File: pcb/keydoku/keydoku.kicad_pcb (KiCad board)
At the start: 2 copper layers, 111 x 99.9 mm, 17 parts

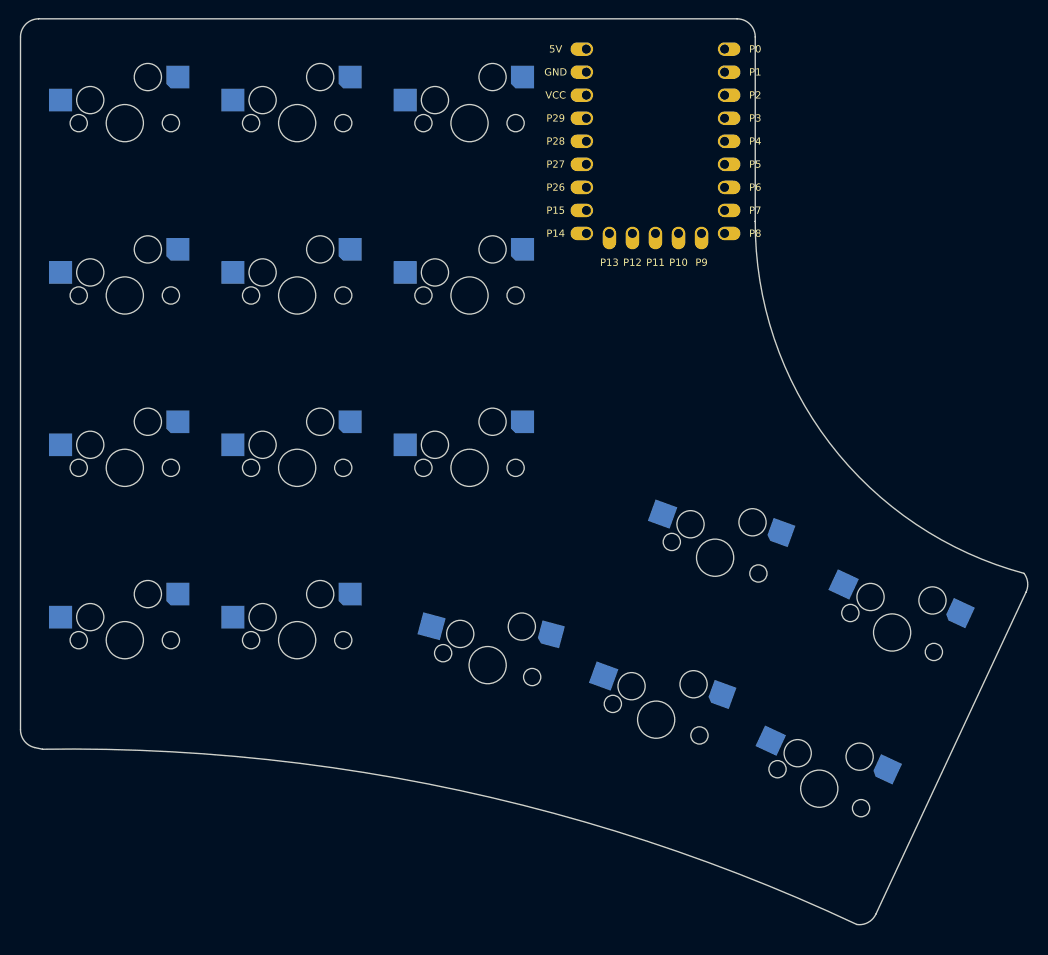
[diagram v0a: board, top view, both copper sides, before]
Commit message: Adding per key LEDs
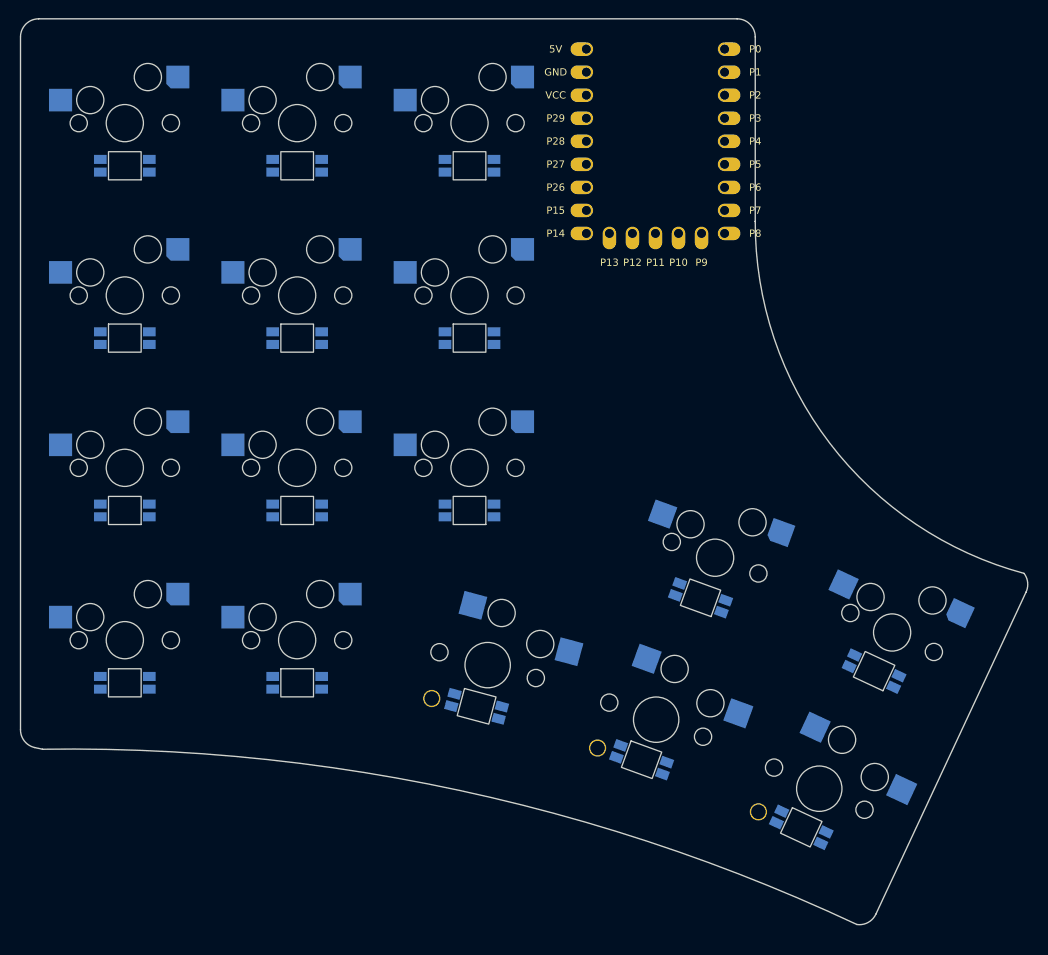
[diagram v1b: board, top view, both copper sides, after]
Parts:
- added LED1: , ceoloide:led_SK6812mini-e (per-keysingle-side), B.Cu at (100.0, 135.7)
- added LED10: , ceoloide:led_SK6812mini-e (per-keysingle-side), B.Cu at (100.0, 116.7)
- added LED11: , ceoloide:led_SK6812mini-e (per-keysingle-side), B.Cu at (119.0, 154.7)
- added LED12: , ceoloide:led_SK6812mini-e (per-keysingle-side), B.Cu at (119.0, 116.7)
- added LED13: , ceoloide:led_SK6812mini-e (per-keysingle-side), B.Cu at (138.0, 116.7)
- added LED14: , ceoloide:led_SK6812mini-e (per-keysingle-side), B.Cu at (138.8, 157.3)
- added LED15: , ceoloide:led_SK6812mini-e (per-keysingle-side), B.Cu at (157.0, 163.2)
- added LED16: , ceoloide:led_SK6812mini-e (per-keysingle-side), B.Cu at (174.6, 170.6)
- added LED2: , ceoloide:led_SK6812mini-e (per-keysingle-side), B.Cu at (100.0, 97.7)
- added LED3: , ceoloide:led_SK6812mini-e (per-keysingle-side), B.Cu at (119.0, 135.7)
- added LED4: , ceoloide:led_SK6812mini-e (per-keysingle-side), B.Cu at (119.0, 97.7)
- added LED5: , ceoloide:led_SK6812mini-e (per-keysingle-side), B.Cu at (138.0, 135.7)
- added LED6: , ceoloide:led_SK6812mini-e (per-keysingle-side), B.Cu at (138.0, 97.7)
- added LED7: , ceoloide:led_SK6812mini-e (per-keysingle-side), B.Cu at (163.5, 145.3)
- added LED8: , ceoloide:led_SK6812mini-e (per-keysingle-side), B.Cu at (182.6, 153.4)
- added LED9: , ceoloide:led_SK6812mini-e (per-keysingle-side), B.Cu at (100.0, 154.7)
- S14, S15, S16: footprint ceoloide:switch_mx -> ceoloide:switch_choc_v1_v2
- moved S12 27.7 mm to (165.1, 140.9), turned to -20 degrees
- moved S14 27.7 mm to (140.0, 152.8), turned to -15 degrees
- moved S13 27.7 mm to (184.6, 149.2), turned to -25 degrees
- moved S15 19.5 mm to (158.6, 158.8), turned to -20 degrees
- moved S16 19.0 mm to (176.6, 166.4)
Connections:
- MCU1 pad 20: P29 -> LED_1
- S1 pad 1: (no net) -> GND
- S1 pad 2: GND -> (no net)
- S10 pad 1: (no net) -> GND
- S10 pad 2: GND -> (no net)
- S11 pad 1: (no net) -> GND
- S11 pad 2: GND -> P2
- S12 pad 1: (no net) -> GND
- S12 pad 2: GND -> (no net)
- S13 pad 1: (no net) -> GND
- S13 pad 2: GND -> (no net)
- S14 pad 1: (no net) -> GND
- S14 pad 2: GND -> (no net)
- S15 pad 1: (no net) -> GND
- S15 pad 2: GND -> (no net)
- S16 pad 1: (no net) -> GND
- S16 pad 2: GND -> (no net)
- S2 pad 1: (no net) -> GND
- S2 pad 2: GND -> (no net)
- S3 pad 1: (no net) -> GND
- S3 pad 2: GND -> (no net)
- S4 pad 1: (no net) -> GND
- S4 pad 2: GND -> (no net)
- S5 pad 1: (no net) -> GND
- S5 pad 2: GND -> (no net)
- S6 pad 1: (no net) -> GND
- S6 pad 2: GND -> (no net)
- S7 pad 1: (no net) -> GND
- S7 pad 2: GND -> (no net)
- S8 pad 1: (no net) -> GND
- S8 pad 2: GND -> (no net)
- S9 pad 1: (no net) -> GND
- S9 pad 2: GND -> (no net)

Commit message: Adding key nets and mounting holes
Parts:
- added H1: , ceoloide:mounting_hole_plated, F.Cu at (100.0, 102.5)
- added H2: , ceoloide:mounting_hole_plated, F.Cu at (138.0, 102.5)
- added H3: , ceoloide:mounting_hole_plated, F.Cu at (100.0, 140.5)
- added H4: , ceoloide:mounting_hole_plated, F.Cu at (171.4, 153.4)
- moved LED14 4.70 mm to (140.0, 152.8)
- moved LED10 4.70 mm to (100.0, 112.0)
- moved LED12 4.70 mm to (119.0, 112.0)
- moved LED13 4.70 mm to (138.0, 112.0)
- moved LED11 4.70 mm to (119.0, 150.0)
- moved LED9 4.70 mm to (100.0, 150.0)
- moved LED15 4.70 mm to (158.6, 158.8)
- moved LED16 4.70 mm to (176.6, 166.4)
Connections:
- S1 pad 2: (no net) -> P9
- S10 pad 2: (no net) -> P13
- S11 pad 2: P2 -> P26
- S12 pad 2: (no net) -> P6
- S13 pad 2: (no net) -> P7
- S14 pad 2: (no net) -> P3
- S15 pad 2: (no net) -> P4
- S16 pad 2: (no net) -> P5
- S2 pad 2: (no net) -> P12
- S3 pad 2: (no net) -> P15
- S4 pad 2: (no net) -> P28
- S5 pad 2: (no net) -> P8
- S6 pad 2: (no net) -> P11
- S7 pad 2: (no net) -> P14
- S8 pad 2: (no net) -> P27
- S9 pad 2: (no net) -> P10
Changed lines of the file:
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@@
 			(chamfer_ratio 0.2)
 			(chamfer bottom_left)
-      (net 0 ""))
+      (net 13 "P9"))
 		(fp_poly
 			(pts
@@
 			(chamfer_ratio 0.2)
 			(chamfer bottom_left)
-      (net 0 ""))
+      (net 16 "P12"))
 		(fp_poly
 			(pts
@@
 			(chamfer_ratio 0.2)
 			(chamfer bottom_left)
-      (net 0 ""))
+      (net 19 "P15"))
 		(fp_poly
 			(pts
@@
 			(chamfer_ratio 0.2)
 			(chamfer bottom_left)
-      (net 0 ""))
+      (net 22 "P28"))
 		(fp_poly
 			(pts
@@
 			(chamfer_ratio 0.2)
 			(chamfer bottom_left)
-      (net 0 ""))
+      (net 12 "P8"))
 		(fp_poly
 			(pts
@@
 			(chamfer_ratio 0.2)
 			(chamfer bottom_left)
-      (net 0 ""))
+      (net 15 "P11"))
 		(fp_poly
 			(pts
@@
 			(chamfer_ratio 0.2)
 			(chamfer bottom_left)
-      (net 0 ""))
+      (net 18 "P14"))
 		(fp_poly
 			(pts
@@
 			(chamfer_ratio 0.2)
 			(chamfer bottom_left)
-      (net 0 ""))
+      (net 21 "P27"))
 		(fp_poly
 			(pts
@@
 			(chamfer_ratio 0.2)
 			(chamfer bottom_left)
-      (net 0 ""))
+      (net 14 "P10"))
 		(fp_poly
 			(pts
@@
 			(chamfer_ratio 0.2)
 			(chamfer bottom_left)
-      (net 0 ""))
+      (net 17 "P13"))
 		(fp_poly
 			(pts
@@
 			(chamfer_ratio 0.2)
 			(chamfer bottom_left)
-      (net 6 "P2"))
+      (net 20 "P26"))
 		(fp_poly
 			(pts
@@
 			(chamfer_ratio 0.2)
 			(chamfer bottom_left)
-      (net 0 ""))
+      (net 10 "P6"))
 		(fp_poly
 			(pts
@@
 			(chamfer_ratio 0.2)
 			(chamfer bottom_left)
-      (net 0 ""))
+      (net 11 "P7"))
 		(fp_poly
 			(pts
@@
     (fp_arc (start 0.8 -3.7) (mid 1.956518 -3.312082) (end 2.5 -2.22) (layer "B.SilkS") (stroke (width 0.15) (type solid)))
     (pad "1" smd rect (at -3.275 -5.95 -15) (size 2.6 2.6) (layers "B.Cu" "B.Paste" "B.Mask") (net 1 "GND"))
-    (pad "2" smd rect (at 8.275 -3.75 -15) (size 2.6 2.6) (layers "B.Cu" "B.Paste" "B.Mask") (net 0 ""))
+    (pad "2" smd rect (at 8.275 -3.75 -15) (size 2.6 2.6) (layers "B.Cu" "B.Paste" "B.Mask") (net 7 "P3"))
     (pad "" np_thru_hole circle (at 5 -3.75 180) (size 3 3) (drill 3) (layers "*.Cu" "*.Mask"))
   )
@@
     (fp_arc (start 0.8 -3.7) (mid 1.956518 -3.312082) (end 2.5 -2.22) (layer "B.SilkS") (stroke (width 0.15) (type solid)))
     (pad "1" smd rect (at -3.275 -5.95 -20) (size 2.6 2.6) (layers "B.Cu" "B.Paste" "B.Mask") (net 1 "GND"))
-    (pad "2" smd rect (at 8.275 -3.75 -20) (size 2.6 2.6) (layers "B.Cu" "B.Paste" "B.Mask") (net 0 ""))
+    (pad "2" smd rect (at 8.275 -3.75 -20) (size 2.6 2.6) (layers "B.Cu" "B.Paste" "B.Mask") (net 8 "P4"))
     (pad "" np_thru_hole circle (at 5 -3.75 175) (size 3 3) (drill 3) (layers "*.Cu" "*.Mask"))
   )
@@
     (fp_arc (start 0.8 -3.7) (mid 1.956518 -3.312082) (end 2.5 -2.22) (layer "B.SilkS") (stroke (width 0.15) (type solid)))
     (pad "1" smd rect (at -3.275 -5.95 -25) (size 2.6 2.6) (layers "B.Cu" "B.Paste" "B.Mask") (net 1 "GND"))
-    (pad "2" smd rect (at 8.275 -3.75 -25) (size 2.6 2.6) (layers "B.Cu" "B.Paste" "B.Mask") (net 0 ""))
+    (pad "2" smd rect (at 8.275 -3.75 -25) (size 2.6 2.6) (layers "B.Cu" "B.Paste" "B.Mask") (net 9 "P5"))
     (pad "" np_thru_hole circle (at 5 -3.75 170) (size 3 3) (drill 3) (layers "*.Cu" "*.Mask"))
   )
@@
   (footprint "ceoloide:led_SK6812mini-e (per-keysingle-side)"
     (layer "B.Cu")
-    (at 100 154.7 0)
+    (at 100 150 0)
     (property "Reference" "LED9"
       (at -4.75 0 90)
@@
   (footprint "ceoloide:led_SK6812mini-e (per-keysingle-side)"
     (layer "B.Cu")
-    (at 100 116.7 0)
+    (at 100 112 0)
     (property "Reference" "LED10"
       (at -4.75 0 90)
@@
   (footprint "ceoloide:led_SK6812mini-e (per-keysingle-side)"
     (layer "B.Cu")
-    (at 119 154.7 0)
+    (at 119 150 0)
     (property "Reference" "LED11"
       (at -4.75 0 90)
@@
   (footprint "ceoloide:led_SK6812mini-e (per-keysingle-side)"
     (layer "B.Cu")
-    (at 119 116.7 0)
+    (at 119 112 0)
     (property "Reference" "LED12"
       (at -4.75 0 90)
@@
   (footprint "ceoloide:led_SK6812mini-e (per-keysingle-side)"
     (layer "B.Cu")
-    (at 138 116.7 0)
+    (at 138 112 0)
     (property "Reference" "LED13"
       (at -4.75 0 90)
@@
   (footprint "ceoloide:led_SK6812mini-e (per-keysingle-side)"
     (layer "B.Cu")
-    (at 138.7835505 157.2898514 -15)
+    (at 140 152.75 -15)
     (property "Reference" "LED14"
       (at -4.75 0 75)
@@
   (footprint "ceoloide:led_SK6812mini-e (per-keysingle-side)"
     (layer "B.Cu")
-    (at 156.96923990000002 163.1794525 -20)
+    (at 158.5767346 158.7628972 -20)
     (property "Reference" "LED15"
       (at -4.75 0 70)
@@
   (footprint "ceoloide:led_SK6812mini-e (per-keysingle-side)"
     (layer "B.Cu")
-    (at 174.57241470000002 170.6316292 -25)
+    (at 176.55872050000002 166.3719826 -25)
     (property "Reference" "LED16"
       (at -4.75 0 65)
@@
     (fp_rect (start -1.8 -1.55) (end 1.8 1.55) (layer "Edge.Cuts") (stroke (width 0.12) (type solid)) (fill none))
   )
+  (footprint "ceoloide:mounting_hole_plated"
+    (layer "F.Cu")
+    (at 100 102.5 0)
+    (property "Reference" "H1"
+      (at 0 3 0)
+      (layer "F.SilkS")
+      hide
+      (effects (font (size 1 1) (thickness 0.15)))
+    )
+    (pad "" thru_hole circle (at 0 0 0) (size 3.8000000000000003 3.8000000000000003) (drill 2.2) (layers "*.Cu" "*.Mask"))
+    (fp_circle (center 0 0) (end -2.1500000000000004 0) (layer "F.CrtYd") (stroke (width 0.05) (type solid)) (fill none))
+    (fp_circle (center 0 0) (end -2.1500000000000004 0) (layer "B.CrtYd") (stroke (width 0.05) (type solid)) (fill none))
+  )
+  (footprint "ceoloide:mounting_hole_plated"
+    (layer "F.Cu")
+    (at 138 102.5 0)
+    (property "Reference" "H2"
+      (at 0 3 0)
+      (layer "F.SilkS")
+      hide
+      (effects (font (size 1 1) (thickness 0.15)))
+    )
+    (pad "" thru_hole circle (at 0 0 0) (size 3.8000000000000003 3.8000000000000003) (drill 2.2) (layers "*.Cu" "*.Mask"))
+    (fp_circle (center 0 0) (end -2.1500000000000004 0) (layer "F.CrtYd") (stroke (width 0.05) (type solid)) (fill none))
+    (fp_circle (center 0 0) (end -2.1500000000000004 0) (layer "B.CrtYd") (stroke (width 0.05) (type solid)) (fill none))
+  )
+  (footprint "ceoloide:mounting_hole_plated"
+    (layer "F.Cu")
+    (at 100 140.5 0)
+    (property "Reference" "H3"
+      (at 0 3 0)
+      (layer "F.SilkS")
+      hide
+      (effects (font (size 1 1) (thickness 0.15)))
+    )
+    (pad "" thru_hole circle (at 0 0 0) (size 3.8000000000000003 3.8000000000000003) (drill 2.2) (layers "*.Cu" "*.Mask"))
+    (fp_circle (center 0 0) (end -2.1500000000000004 0) (layer "F.CrtYd") (stroke (width 0.05) (type solid)) (fill none))
+    (fp_circle (center 0 0) (end -2.1500000000000004 0) (layer "B.CrtYd") (stroke (width 0.05) (type solid)) (fill none))
+  )
+  (footprint "ceoloide:mounting_hole_plated"
+    (layer "F.Cu")
+    (at 171.44 153.42000000000002 0)
+    (property "Reference" "H4"
+      (at 0 3 0)
+      (layer "F.SilkS")
+      hide
+      (effects (font (size 1 1) (thickness 0.15)))
+    )
+    (pad "" thru_hole circle (at 0 0 0) (size 3.8000000000000003 3.8000000000000003) (drill 2.2) (layers "*.Cu" "*.Mask"))
+    (fp_circle (center 0 0) (end -2.1500000000000004 0) (layer "F.CrtYd") (stroke (width 0.05) (type solid)) (fill none))
+    (fp_circle (center 0 0) (end -2.1500000000000004 0) (layer "B.CrtYd") (stroke (width 0.05) (type solid)) (fill none))
+  )
   (gr_line (start 88.5 159.88473723721162) (end 88.5 83.5) (layer Edge.Cuts) (stroke (width 0.15) (type default)))

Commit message: Moving MCU silkscreen inside and adding choc outline
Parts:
- moved H4 8.75 mm to (174.6, 145.2)
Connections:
- S11 pad 2: P26 -> P28
- S12 pad 2: P6 -> P7
- S13 pad 2: P7 -> P6
- S4 pad 2: P28 -> P26
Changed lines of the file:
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@@
   (title_block
     (title "keydoku")
-    (date "2024-10-29")
+    (date "2024-11-01")
     (rev "v1.0.0")
     (company "Unknown")
@@
         (fp_rect (start -9 -11.75) (end 9 11.75)
           (stroke (width 0.12) (type solid)) (fill none) (layer Dwgs.User))
-        (fp_text user P0 (at 11 -10.16)    (layer F.SilkS) (effects (font (size 0.8 0.8) (thickness 0.15))))
-        (fp_text user P1 (at 11 -7.62)     (layer F.SilkS) (effects (font (size 0.8 0.8) (thickness 0.15))))
-        (fp_text user P2 (at 11 -5.08)     (layer F.SilkS) (effects (font (size 0.8 0.8) (thickness 0.15))))
-        (fp_text user P3 (at 11 -2.54)     (layer F.SilkS) (effects (font (size 0.8 0.8) (thickness 0.15))))
-        (fp_text user P4 (at 11 0)         (layer F.SilkS) (effects (font (size 0.8 0.8) (thickness 0.15))))
-        (fp_text user P5 (at 11 2.54)      (layer F.SilkS) (effects (font (size 0.8 0.8) (thickness 0.15))))
-        (fp_text user P6 (at 11 5.08)      (layer F.SilkS) (effects (font (size 0.8 0.8) (thickness 0.15))))
-        (fp_text user P7 (at 11 7.62)      (layer F.SilkS) (effects (font (size 0.8 0.8) (thickness 0.15))))
-        (fp_text user P8 (at 11 10.16)     (layer F.SilkS) (effects (font (size 0.8 0.8) (thickness 0.15))))
-        (fp_text user P9  (at 5.08 13.36)  (layer F.SilkS) (effects (font (size 0.8 0.8) (thickness 0.15))))
-        (fp_text user P10 (at 2.54 13.36)  (layer F.SilkS) (effects (font (size 0.8 0.8) (thickness 0.15))))
-        (fp_text user P11 (at 0 13.36)               (layer F.SilkS) (effects (font (size 0.8 0.8) (thickness 0.15))))
-        (fp_text user P12 (at -2.54 13.36)  (layer F.SilkS) (effects (font (size 0.8 0.8) (thickness 0.15))))
-        (fp_text user P13 (at -5.08 13.36)  (layer F.SilkS) (effects (font (size 0.8 0.8) (thickness 0.15))))
-        (fp_text user P14 (at -11 10.16)    (layer F.SilkS) (effects (font (size 0.8 0.8) (thickness 0.15))))
-        (fp_text user P15 (at -11 7.62)     (layer F.SilkS) (effects (font (size 0.8 0.8) (thickness 0.15))))
-        (fp_text user P26 (at -11 5.08)     (layer F.SilkS) (effects (font (size 0.8 0.8) (thickness 0.15))))
-        (fp_text user P27 (at -11 2.54)     (layer F.SilkS) (effects (font (size 0.8 0.8) (thickness 0.15))))
-        (fp_text user P28 (at -11 0)        (layer F.SilkS) (effects (font (size 0.8 0.8) (thickness 0.15))))
-        (fp_text user P29 (at -11 -2.54)    (layer F.SilkS) (effects (font (size 0.8 0.8) (thickness 0.15))))
-        (fp_text user VCC (at -11 -5.08)    (layer F.SilkS) (effects (font (size 0.8 0.8) (thickness 0.15))))
-        (fp_text user GND (at -11 -7.62)    (layer F.SilkS) (effects (font (size 0.8 0.8) (thickness 0.15))))
-        (fp_text user 5V  (at -11 -10.16)   (layer F.SilkS) (effects (font (size 0.8 0.8) (thickness 0.15))))
+        (fp_text user P0 (at 5 -10.16)    (layer F.SilkS) (effects (font (size 0.8 0.8) (thickness 0.15))))
+        (fp_text user P1 (at 5 -7.62)     (layer F.SilkS) (effects (font (size 0.8 0.8) (thickness 0.15))))
+        (fp_text user P2 (at 5 -5.08)     (layer F.SilkS) (effects (font (size 0.8 0.8) (thickness 0.15))))
+        (fp_text user P3 (at 5 -2.54)     (layer F.SilkS) (effects (font (size 0.8 0.8) (thickness 0.15))))
+        (fp_text user P4 (at 5 0)         (layer F.SilkS) (effects (font (size 0.8 0.8) (thickness 0.15))))
+        (fp_text user P5 (at 5 2.54)      (layer F.SilkS) (effects (font (size 0.8 0.8) (thickness 0.15))))
+        (fp_text user P6 (at 5 5.08)      (layer F.SilkS) (effects (font (size 0.8 0.8) (thickness 0.15))))
+        (fp_text user P7 (at 5 7.62)      (layer F.SilkS) (effects (font (size 0.8 0.8) (thickness 0.15))))
+        (fp_text user P8 (at 5 10.16)     (layer F.SilkS) (effects (font (size 0.8 0.8) (thickness 0.15))))
+        (fp_text user P9  (at 5.08 8.69)  (layer F.SilkS) (effects (font (size 0.8 0.8) (thickness 0.15))))
+        (fp_text user P10 (at 2.54 8.69)  (layer F.SilkS) (effects (font (size 0.8 0.8) (thickness 0.15))))
+        (fp_text user P11 (at 0 8.69)               (layer F.SilkS) (effects (font (size 0.8 0.8) (thickness 0.15))))
+        (fp_text user P12 (at -2.54 8.69)  (layer F.SilkS) (effects (font (size 0.8 0.8) (thickness 0.15))))
+        (fp_text user P13 (at -5.08 8.69)  (layer F.SilkS) (effects (font (size 0.8 0.8) (thickness 0.15))))
+        (fp_text user P14 (at -5 10.16)    (layer F.SilkS) (effects (font (size 0.8 0.8) (thickness 0.15))))
+        (fp_text user P15 (at -5 7.62)     (layer F.SilkS) (effects (font (size 0.8 0.8) (thickness 0.15))))
+        (fp_text user P26 (at -5 5.08)     (layer F.SilkS) (effects (font (size 0.8 0.8) (thickness 0.15))))
+        (fp_text user P27 (at -5 2.54)     (layer F.SilkS) (effects (font (size 0.8 0.8) (thickness 0.15))))
+        (fp_text user P28 (at -5 0)        (layer F.SilkS) (effects (font (size 0.8 0.8) (thickness 0.15))))
+        (fp_text user P29 (at -5 -2.54)    (layer F.SilkS) (effects (font (size 0.8 0.8) (thickness 0.15))))
+        (fp_text user VCC (at -5 -5.08)    (layer F.SilkS) (effects (font (size 0.8 0.8) (thickness 0.15))))
+        (fp_text user GND (at -5 -7.62)    (layer F.SilkS) (effects (font (size 0.8 0.8) (thickness 0.15))))
+        (fp_text user 5V  (at -5 -10.16)   (layer F.SilkS) (effects (font (size 0.8 0.8) (thickness 0.15))))
         (pad 1 thru_hole oval (at 7.62 -10.16 180)        (size 2.5 1.5) (drill 1 (offset -0.5 0)) (layers *.Cu *.Mask) (net 4 "P0"))
         (pad 2 thru_hole oval (at 7.62 -7.62 180)         (size 2.5 1.5) (drill 1 (offset -0.5 0)) (layers *.Cu *.Mask) (net 5 "P1"))
@@
 			(chamfer_ratio 0.2)
 			(chamfer bottom_left)
-      (net 22 "P28"))
+      (net 20 "P26"))
 		(fp_poly
 			(pts
@@
 			(chamfer_ratio 0.2)
 			(chamfer bottom_left)
-      (net 20 "P26"))
+      (net 22 "P28"))
 		(fp_poly
 			(pts
@@
 			(chamfer_ratio 0.2)
 			(chamfer bottom_left)
-      (net 10 "P6"))
+      (net 11 "P7"))
 		(fp_poly
 			(pts
@@
 			(chamfer_ratio 0.2)
 			(chamfer bottom_left)
-      (net 11 "P7"))
+      (net 10 "P6"))
 		(fp_poly
 			(pts
@@
   (footprint "ceoloide:mounting_hole_plated"
     (layer "F.Cu")
-    (at 171.44 153.42000000000002 0)
+    (at 174.575 145.25 0)
     (property "Reference" "H4"
       (at 0 3 0)

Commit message: Removing User.Drawings from PCB
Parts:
- removed H1, H2, H3, H4: , ceoloide:mounting_hole_plated
- added MH1: , ceoloide:mounting_hole_npth, F.Cu at (100.0, 102.5)
- added MH2: , ceoloide:mounting_hole_npth, F.Cu at (138.0, 102.5)
- added MH3: , ceoloide:mounting_hole_npth, F.Cu at (100.0, 140.5)
- added MH4: , ceoloide:mounting_hole_npth, F.Cu at (174.6, 145.2)
- moved LED14 4.70 mm to (138.8, 157.3)
- moved LED10 4.70 mm to (100.0, 116.7)
- moved LED12 4.70 mm to (119.0, 116.7)
- moved LED13 4.70 mm to (138.0, 116.7)
- moved LED11 4.70 mm to (119.0, 154.7)
- moved LED9 4.70 mm to (100.0, 154.7)
- moved LED15 4.70 mm to (157.0, 163.2)
- moved LED16 4.70 mm to (174.6, 170.6)
